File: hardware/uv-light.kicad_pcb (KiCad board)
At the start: 2 copper layers, 15 x 25 mm, 27 parts, among them P1 CON-SENSOR2, P2 DEBUG, P3 BOOT, U1 XMC1XXX24, U2 VEML6070, U3 DRILL, U4 DRILL, U5 DRILL, U6 DRILL

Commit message: Add "tinkerforge.com" to silkscreen
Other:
- board text added: "tinkerforge.com"
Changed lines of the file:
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@@
     (links 52)
     (no_connects 0)
-    (area 13.796426 74.544999 145.255001 194.575)
+    (area 129.209499 75.209499 144.590501 100.590501)
     (thickness 1.6)
-    (drawings 11)
+    (drawings 12)
     (tracks 201)
     (zones 0)
@@
       (xy 2.48217 3.513666) (xy 2.482863 3.409859) (xy 2.482863 3.409859)) (layer B.SilkS) (width 0.1))
   )
+  (gr_text tinkerforge.com (at 141.72 87.9 270) (layer B.SilkS)
+    (effects (font (size 0.7 0.7) (thickness 0.15)) (justify mirror))
+  )
   (gr_text Status (at 136.9 76.4) (layer F.SilkS)

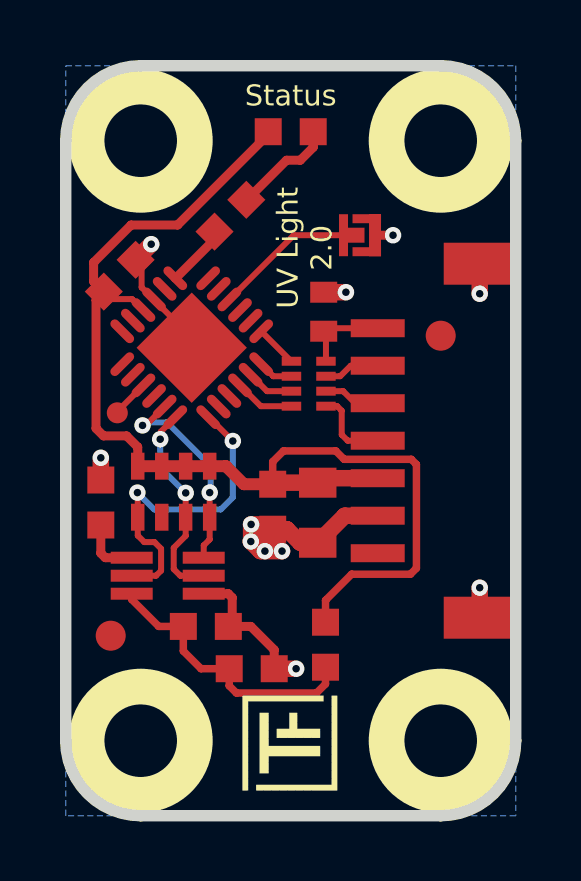
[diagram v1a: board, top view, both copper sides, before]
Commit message: change sensor to veml6075
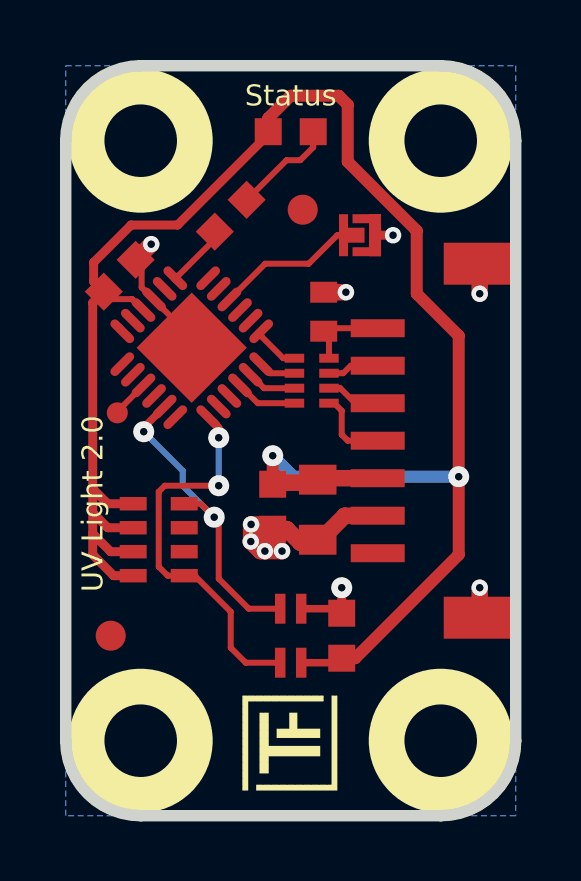
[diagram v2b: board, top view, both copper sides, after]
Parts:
- removed C6: 100nF, kicad-libraries:C0603F
- removed R2: 10, kicad-libraries:R0603F
- removed R3: 1k, kicad-libraries:R0603F
- C1: value 10uF -> 220pF; footprint kicad-libraries:C0805 -> kicad-libraries:C0402E
- C2: value 100nF -> 10uF; footprint kicad-libraries:C0603F -> kicad-libraries:C0805
- C3: value 10µF -> 1uF
- C4: value 220pF -> 100nF; footprint kicad-libraries:C0402E -> kicad-libraries:C0603F
- C5: value 1uF -> 100nF
- R1: value 270k -> 1k
- RP1: value 2k2 -> 82; footprint kicad-libraries:0603X4 -> kicad-libraries:4X0402
- RP2: value 82 -> 2k2; footprint kicad-libraries:4X0402 -> kicad-libraries:0603X4
- U2: value VEML6070 -> VEML6075; footprint kicad-libraries:OPLGA6 -> OPLGA4
- moved R1 10.5 mm to (134.9, 80.4), turned to 45 degrees
- moved RP2 7.21 mm to (132.5, 91.2)
- moved C4 6.91 mm to (131.2, 82.4), turned to 225 degrees
- moved C1 6.70 mm to (138.0, 83.6), turned to 270 degrees
- moved Fiducial_Mark 6.23 mm to (137.3, 80.2)
- moved RP1 5.90 mm to (137.6, 85.9), turned to 90 degrees
- moved C3 5.45 mm to (136.3, 90.1), turned to 90 degrees
- moved C2 5.39 mm to (137.8, 90.2), turned to 90 degrees
- moved C5 4.88 mm to (138.6, 94.4), turned to 270 degrees
- moved U2 4.56 mm to (136.9, 94.4), turned to 270 degrees
- moved VAL 0.73 mm to (136.9, 87.9)
- moved G*** 0.09 mm to (136.9, 80.4)
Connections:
- C1 pad 2: VCC -> Net-(C1-Pad2)
- C2 pad 2: Net-(C2-Pad2) -> VCC
- C3 pad 2: Net-(C2-Pad2) -> VCC
- C4 pad 2: Net-(C4-Pad2) -> VCC
- P1 pad 1: Net-(P1-Pad1) -> (no net)
- P1 pad 7: Net-(C4-Pad2) -> Net-(C1-Pad2)
- R1 pad 2: GND -> Net-(D1-Pad2)
- RP1 pad 1: VCC -> Net-(P1-Pad4)
- RP1 pad 2: VCC -> Net-(P1-Pad5)
- RP1 pad 3: VCC -> Net-(P1-Pad6)
- RP1 pad 4: VCC -> Net-(C1-Pad2)
- RP1 pad 5: SCL -> S-MISO
- RP1 pad 6: Net-(RP1-Pad6) -> S-MOSI
- RP1 pad 7: ACK -> S-CLK
- RP1 pad 8: SDA -> S-CS
- RP2 pad 1: Net-(P1-Pad4) -> VCC
- RP2 pad 2: Net-(P1-Pad5) -> VCC
- RP2 pad 3: Net-(P1-Pad6) -> VCC
- RP2 pad 4: Net-(C4-Pad2) -> VCC
- RP2 pad 5: S-MISO -> SCL
- RP2 pad 6: S-MOSI -> (no net)
- RP2 pad 7: S-CLK -> (no net)
- RP2 pad 8: S-CS -> SDA
- U1 pad 11: Net-(U1-Pad11) -> (no net)
- U1 pad 12: Net-(U1-Pad12) -> (no net)
- U1 pad 13: Net-(U1-Pad13) -> (no net)
- U1 pad 14: Net-(U1-Pad14) -> (no net)
- U1 pad 16: Net-(U1-Pad16) -> (no net)
- U1 pad 18: ACK -> (no net)
- U1 pad 2: Net-(U1-Pad2) -> (no net)
- U1 pad 20: Net-(U1-Pad20) -> (no net)
- U1 pad 21: Net-(U1-Pad21) -> (no net)
- U1 pad 3: Net-(U1-Pad3) -> (no net)
- U1 pad 5: Net-(U1-Pad5) -> (no net)
- U1 pad 6: Net-(U1-Pad6) -> (no net)
- U1 pad 7: Net-(R3-Pad1) -> Net-(R1-Pad1)
- U1 pad 8: Net-(U1-Pad8) -> (no net)
- U2 pad 2: ACK -> SDA
- U2 pad 3: SDA -> SCL
- U2 pad 4: Net-(R1-Pad1) -> VCC
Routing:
- net VCC: track 39.2 -> 63.5 mm, vias 0 -> 2
- net Net-(C2-Pad2): track 9.44 -> 0.00 mm
- net ACK: track 6.88 -> 0.00 mm, vias 2 -> 0
- net GND: track 29.2 -> 25.4 mm, vias 11 -> 10
- net SDA: track 7.07 -> 10.7 mm
- net Net-(C1-Pad2): track 0.00 -> 2.92 mm
- net Net-(C4-Pad2): track 2.87 -> 0.00 mm
- net SCL: track 10.8 -> 13.1 mm
- net Net-(R3-Pad1): track 2.10 -> 0.00 mm
- net Net-(P1-Pad5): track 1.89 -> 2.58 mm
